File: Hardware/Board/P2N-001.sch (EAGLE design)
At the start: 36 parts, among them IC1 4053N, IC2 74LS157N, IC3 LTC485N, IC4 74LS07N, IC5 LTC485N, K1 G5V-2, K2 G5V1, T1 2SC1815, T2 2SC1815

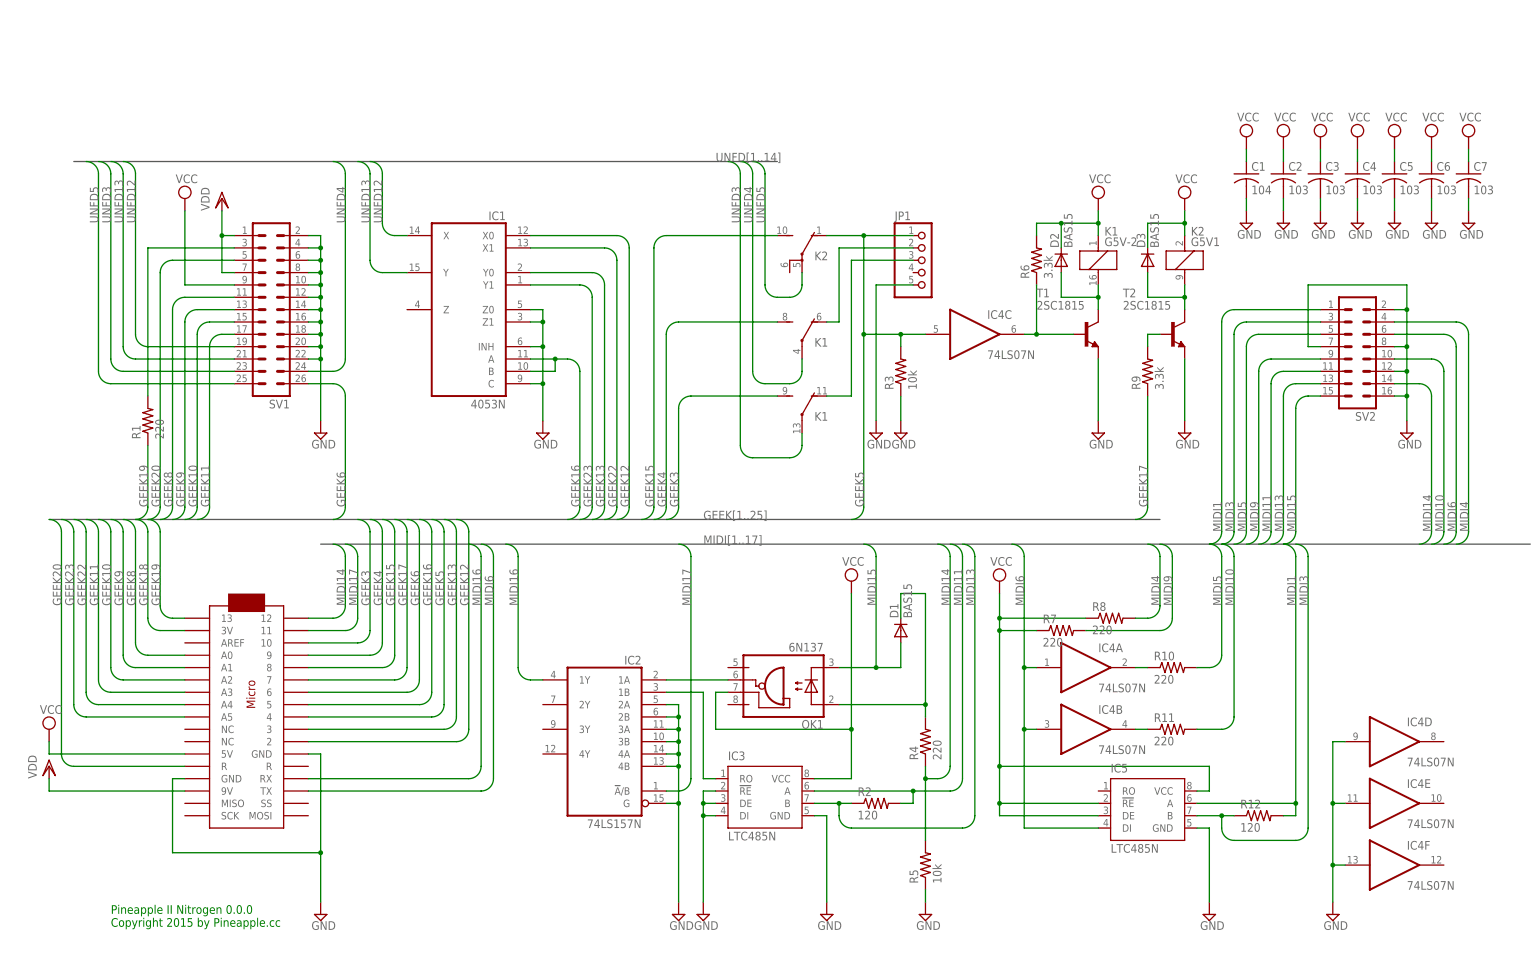
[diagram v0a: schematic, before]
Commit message: Some pinouts were replaced.
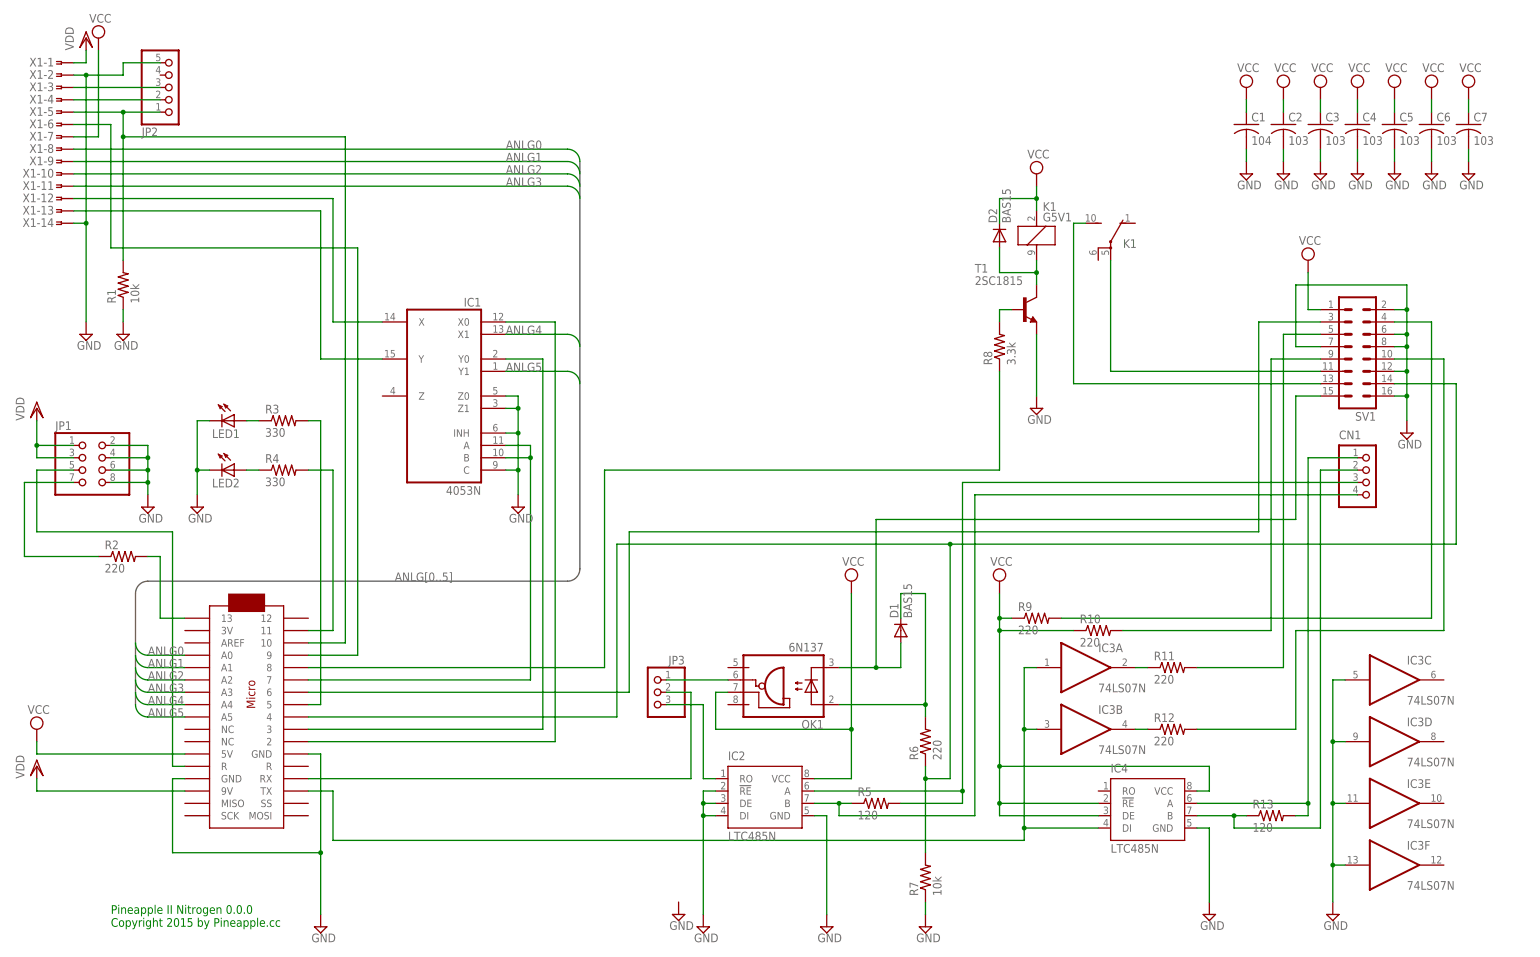
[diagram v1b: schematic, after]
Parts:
- removed D3: BAS15, diode:BAS15
- removed IC5: LTC485N, linear-technology:LTC485N
- removed K2: G5V1, relay:G5V1
- removed SV2: (no value), con-ml:ML16L
- removed T2: 2SC1815, transistor:2SC1815
- added CN1: (no value), jst-ph:B4B-PH-K-S
- added JP2: (no value), pinhead:PINHD-1X5
- added JP3: (no value), pinhead:PINHD-1X3
- added LED1, LED2: (no value), led:LED3MM
- added R13: 120, resistor:R-US_0204/5
- added X1: (no value), con-hirose-dxlm:HIROSE-DXLM
- IC2: value 74LS157N -> LTC485N; device 74xx-us:74LS157N -> linear-technology:LTC485N
- IC3: value LTC485N -> 74LS07N; device linear-technology:LTC485N -> 74xx-us:74LS07N
- IC4: value 74LS07N -> LTC485N; device 74xx-us:74LS07N -> linear-technology:LTC485N
- JP1: device pinhead:PINHD-1X5 -> pinhead:PINHD-2X4
- K1: value G5V-2 -> G5V1; device relay:G5V-2 -> relay:G5V1
- R1, R7: value 220 -> 10k
- R12, R2: value 120 -> 220
- R3: value 10k -> 330
- R4: value 220 -> 330
- R5: value 10k -> 120
- R6, R9: value 3.3k -> 220
- R8: value 220 -> 3.3k
- SV1: device con-ml:ML26L -> con-ml:ML16L
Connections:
- net GEEK12 renamed N$23
- net GEEK13 renamed N$19
- net GEEK22 renamed ANLG4
- net GEEK23 renamed ANLG5
- removed net GEEK10: MC1.A2, SV1.15
- removed net GEEK11: MC1.A3, SV1.17
- removed net GEEK15: K22.S, MC1.8
- removed net GEEK17: MC1.7, R9.1
- removed net GEEK18: MC1.3V
- removed net GEEK19: MC1.13, R1.1
- removed net GEEK20: MC1.R@1, SV1.5
- removed net GEEK3: K12.S, MC1.10
- removed net GEEK4: K11.S, MC1.9
- removed net GEEK5: IC4C.I, JP1.1, K22.O, MC1.4, R3.2
- removed net GEEK6: MC1.6, SV1.26
- removed net GEEK8: MC1.A0, SV1.11
- removed net GEEK9: MC1.A1, SV1.13
- removed net MIDI10: R11.2, SV2.10
- removed net MIDI16: IC2A.1Y, MC1.RX
- removed net MIDI17: IC2A.!A!/B, MC1.11
- removed net MIDI4: R8.2, SV2.4
- removed net MIDI5: R10.2, SV2.5
- removed net MIDI9: R7.2, SV2.9
- removed net UNFD12: IC1A.X, SV1.19
- removed net UNFD13: IC1A.Y, SV1.21
- removed net UNFD3: K12.P, SV1.23
- removed net UNFD4: K11.P, SV1.24
- removed net UNFD5: K22.P, SV1.25
- new net ANLG0: MC1.A0, X1-8.1
- new net ANLG1: MC1.A1, X1-9.1
- new net ANLG2: MC1.A2, X1-10.1
- new net ANLG3: MC1.A3, X1-11.1
- new net N$10: R11.2, SV1.5
- new net N$11: R10.2, SV1.9
- new net N$12: R9.2, SV1.4
- new net N$13: R12.2, SV1.10
- new net N$14: K12.S, SV1.13
- new net N$16: K12.P, SV1.11
- new net N$17: LED1.A, R3.1
- new net N$18: LED2.A, R4.1
- new net N$20: MC1.5, R3.2
- new net N$21: MC1.11, R4.2
- new net N$22: MC1.8, R8.1
- new net N$24: JP2.1, MC1.10, R1.2, X1-5.1
- new net N$25: JP2.2, X1-4.1
- new net N$26: JP2.3, X1-3.1
- new net N$27: MC1.9, X1-6.1
- new net N$28: IC1A.X, X1-12.1
- new net N$29: IC1A.Y, X1-13.1
- net GEEK16: now also MC1.7; no longer MC1.5
- net GND: now also IC2.!RE, IC2.DE, IC2.DI, IC2.GND, IC3C.I, IC3D.I, IC3E.I, IC3F.I, IC4.GND, JP1.2, JP1.4, JP1.6, JP1.8, JP2.5, LED1.C, LED2.C, R1.1, R7.1, SV1.7, X1-14.1, X1-2.1; no longer IC2A.2A, IC2A.2B, IC2A.3A, IC2A.3B, IC2A.4A, IC2A.4B, IC2A.G, IC3.!RE, IC3.DE, IC3.DI, IC3.GND, IC4D.I, IC4E.I, IC4F.I, IC5.GND, JP1.5, R3.1, R5.1, SV1.10, SV1.14, SV1.18, SV1.20, SV1.22, SV1.4, SV2.12, SV2.16, SV2.2, SV2.7, SV2.8, T2.E
- net MIDI1: now also CN1.1, IC4.A, R13.2; no longer IC5.A, R12.2, SV2.1
- net MIDI11: now also CN1.3, IC2.A, R5.2; no longer IC3.A, R2.2, SV2.11
- net MIDI13: now also CN1.4, IC2.B, R5.1; no longer IC3.B, R2.1, SV2.13
- net MIDI14: now also MC1.4, R6.1, R7.2, SV1.14; no longer MC1.12, R4.1, R5.2, SV2.14
- net MIDI15: now also SV1.15; no longer SV2.15
- net MIDI3: now also CN1.2, IC4.B, R13.1; no longer IC5.B, R12.1, SV2.3
- net MIDI6: now also IC3A.I, IC3B.I, IC4.DI; no longer IC4A.I, IC4B.I, IC5.DI, SV2.6
- net MIDIRX: now also JP3.1; no longer IC2A.1A
- net N$1: now also IC3B.O, R12.1; no longer IC4B.O, R11.1
- net N$15: now also R6.2; no longer R4.2
- net N$2: now also IC3A.O, R11.1; no longer IC4A.O, R10.1
- net N$3: now also JP1.5, MC1.R@1; no longer R1.2, SV1.3
- net N$4: now also JP1.7, R2.1; no longer D2.A, K1A.2, T1.C
- net N$5: now also MC1.13, R2.2; no longer JP1.2, K11.O
- net N$6: now also D2.A, K11.2, T1.C; no longer D3.A, K21.2, T2.C
- net N$7: now also JP3.2, MC1.RX; no longer IC4C.O, R6.1, T1.B
- net N$8: now also R8.2, T1.B; no longer R9.2, T2.B
- net N$9: now also MC1.6, SV1.3; no longer JP1.3, K12.O
- net VCC: now also IC2.VCC, IC4.!RE, IC4.DE, IC4.VCC, K11.1, R10.1, R9.1, SV1.1, X1-7.1; no longer D3.C, IC3.VCC, IC5.!RE, IC5.DE, IC5.VCC, K1A.1, K21.1, R6.2, R7.1, R8.1, SV1.9
- net VDD: now also JP1.1, JP1.3, X1-1.1; no longer SV1.1, SV1.7
- net XMIDIRX: now also IC2.RO, JP3.3; no longer IC2A.1B, IC3.RO
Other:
- moved on the sheet: C1, C2, C3, C4, C5, C6, C7, D2, IC1, R1, R10, R11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

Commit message: New board design.
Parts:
- removed LED1, LED2: (no value), led:LED3MM
- added JP4: (no value), pinhead:PINHD-1X3
- JP2: device pinhead:PINHD-1X5 -> pinhead:PINHD-1X5/90
- JP3: device pinhead:PINHD-1X3 -> pinhead:PINHD-1X4
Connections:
- net GND: now also JP3.2, JP3.4; no longer LED1.C, LED2.C
- net MIDIRX: now also JP4.1; no longer JP3.1
- net N$17: now also JP3.1; no longer LED1.A
- net N$18: now also JP3.3; no longer LED2.A
- net N$7: now also JP4.2; no longer JP3.2
- net XMIDIRX: now also JP4.3; no longer JP3.3
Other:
- moved on the sheet: R3
